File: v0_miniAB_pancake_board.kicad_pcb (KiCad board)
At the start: 2 copper layers, 51 x 38.3 mm, 15 parts, among them J1 E_STEPPER, J10 FAN0_V_JUMPER, J11 FAN1_V_JUMPER, J12 RGB LED, J13 BLTOUCH, J2 HEATER, J3 THERM, J4 PART FAN, J5 PART FAN, J6 HOTEND FAN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

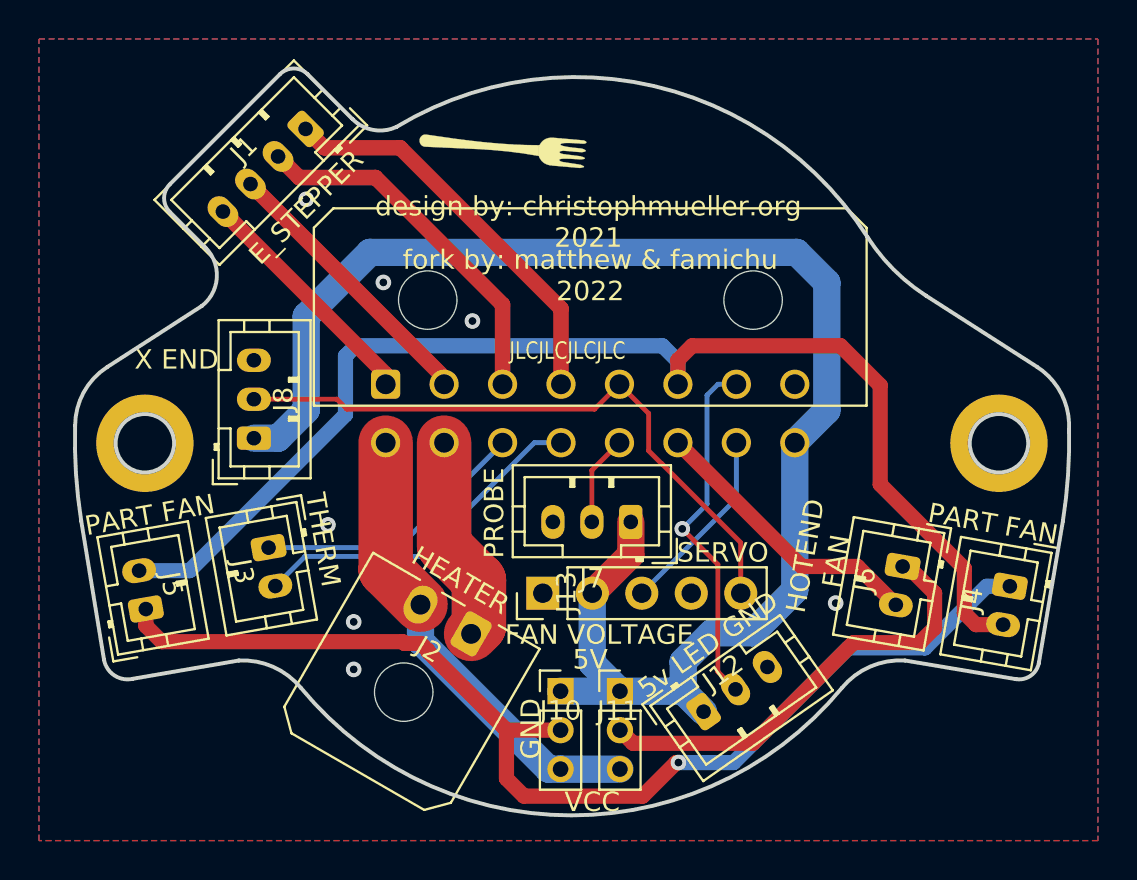
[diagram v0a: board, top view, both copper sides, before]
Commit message: Fixing safety issues
* The heater connector was at an angle that could cause cable interference with the X endstop on the V0
* The fan voltage selector is now a 2x3 pin connector
* The X end stop position was switched -- now fixed
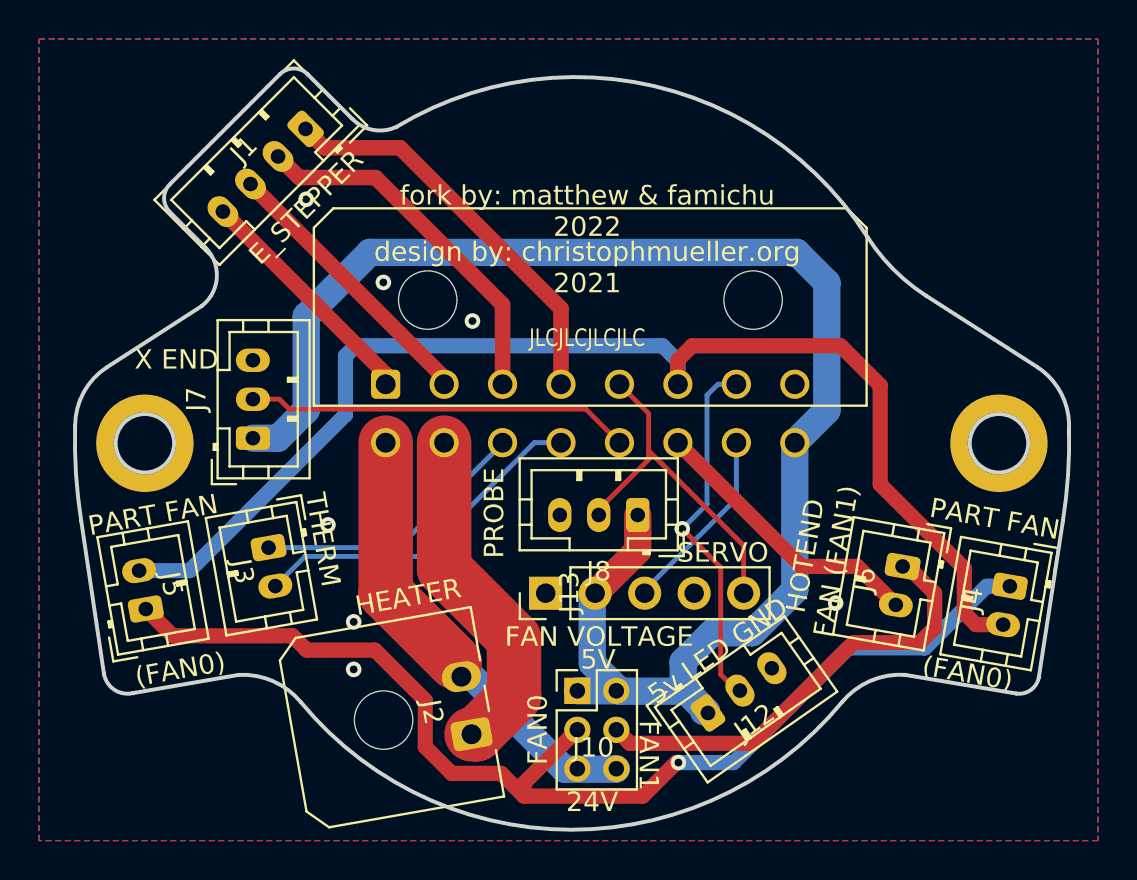
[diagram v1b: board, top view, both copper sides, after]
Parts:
- removed J11: FAN1_V_JUMPER, Connector_PinHeader_2.00mm:PinHeader_1x03_P2.00mm_Vertical
- J10: footprint Connector_PinHeader_2.00mm:PinHeader_1x03_P2.00mm_Vertical -> Connector_PinHeader_2.00mm:PinHeader_2x03_P2.00mm_Vertical
- moved J8 20.1 mm to (103.4, 103.7), turned to 180 degrees
- moved J7 19.9 mm to (83.6, 99.7), turned to 90 degrees
- moved J2 5.15 mm to (94.8, 114.9), turned to 100 degrees
- moved J10 0.86 mm to (100.3, 112.7)
- moved J12 0.24 mm to (107.0, 113.8)
- moved J13 0.15 mm to (98.7, 107.7)
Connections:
- J10 pad 2: /VFAN0 -> +5V
- J10 pad 3: +24V -> /VFAN0
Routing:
- net /sw0: track 4.65 -> 19.7 mm
- net /sw1: track 32.8 -> 17.7 mm
- net /heat_gnd: track 10.7 -> 17.5 mm
- net +24V: track 23.9 -> 22.7 mm
- net /VFAN0: track 57.6 -> 58.7 mm
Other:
- board size 51 x 38.3 mm -> 51 x 39.1 mm
- board text added: "24V"
- board text added: "FAN0"
- board text added: "FAN1"
- board text added: "HOTEND FAN (FAN1)"
- board text added: "PART FAN (FAN0)"
- board text removed: "GND"
- board text removed: "HOTEND FAN"
- board text removed: "PART FAN"
- board text removed: "VCC"

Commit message: Fixing Silkscreen
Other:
- board text added: "24V HEAT_GND TH0 TH1 X-END FAN1 SERVO 5V"
- board text added: "A+ A- B+ B- PROBE FAN0 LED GND"
- board text removed: "24V HEAT_GND TH0 TH1 PROBE FAN1 SERVO 5V"
- board text removed: "A+ A- B+ B- X END FAN0 LED GND"
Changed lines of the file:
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@@
     (property "Sheetname" "")
     (attr through_hole)
-    (fp_text reference "J8" (at 2 -2.9) (layer "F.SilkS")
+    (fp_text reference "J8" (at 2 1.5748) (layer "F.SilkS")
       (effects (font (size 1 1) (thickness 0.15)))
     )
@@
     (property "Sheetname" "")
     (attr through_hole)
-    (fp_text reference "J7" (at 2 -2.9 90) (layer "F.SilkS")
+    (fp_text reference "J7" (at 2 1.7184 90) (layer "F.SilkS")
       (effects (font (size 1 1) (thickness 0.15)))
     )
@@
     (effects (font (size 2 2) (thickness 0.3)) (justify mirror))
   )
-  (gr_text "A+\n\nA-\n\nB+\n\nB-\n\nX END\n\nFAN0\n\nLED\n\nGND" (at 102.3112 93.8276 90) (layer "B.SilkS")
+  (gr_text "A+\n\nA-\n\nB+\n\nB-\n\nPROBE\n\nFAN0\n\nLED\n\nGND" (at 102.3112 93.8276 90) (layer "B.SilkS")
     (effects (font (size 1 1) (thickness 0.15)) (justify left mirror))
   )
-  (gr_text "24V\n\nHEAT_GND\n\nTH0\n\nTH1\n\nPROBE\n\nFAN1\n\nSERVO\n\n5V" (at 101.7016 100.584 90) (layer "B.SilkS")
+  (gr_text "24V\n\nHEAT_GND\n\nTH0\n\nTH1\n\nX-END\n\nFAN1\n\nSERVO\n\n5V" (at 102.362 101.092 90) (layer "B.SilkS")
     (effects (font (size 1 1) (thickness 0.15)) (justify left mirror))
   )
@@
     (effects (font (size 1 1) (thickness 0.15)) (justify mirror))
   )
-  (gr_text "(as seen \nfrom this \nside)" (at 116.0272 100.5332 90) (layer "B.SilkS")
+  (gr_text "(as seen \nfrom this \nside)" (at 116.332 100.584 90) (layer "B.SilkS")
     (effects (font (size 1 1) (thickness 0.15)) (justify mirror))
   )
